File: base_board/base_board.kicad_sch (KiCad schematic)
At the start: 54 parts, among them J1 Conn_ARM_JTAG_SWD_20, J2 Conn_01x20_Pin, J3 Conn_01x20_Socket, SW1 SW_Push, U1 STM32F446ZEJx, U2 IS42S16400J-xT, U3 BMI270, U4 USB_C_Receptacle_USB2.0, U5 10p, U6 10p, U7 LD3985M33R_SOT23, Y1 Crystal_GND24

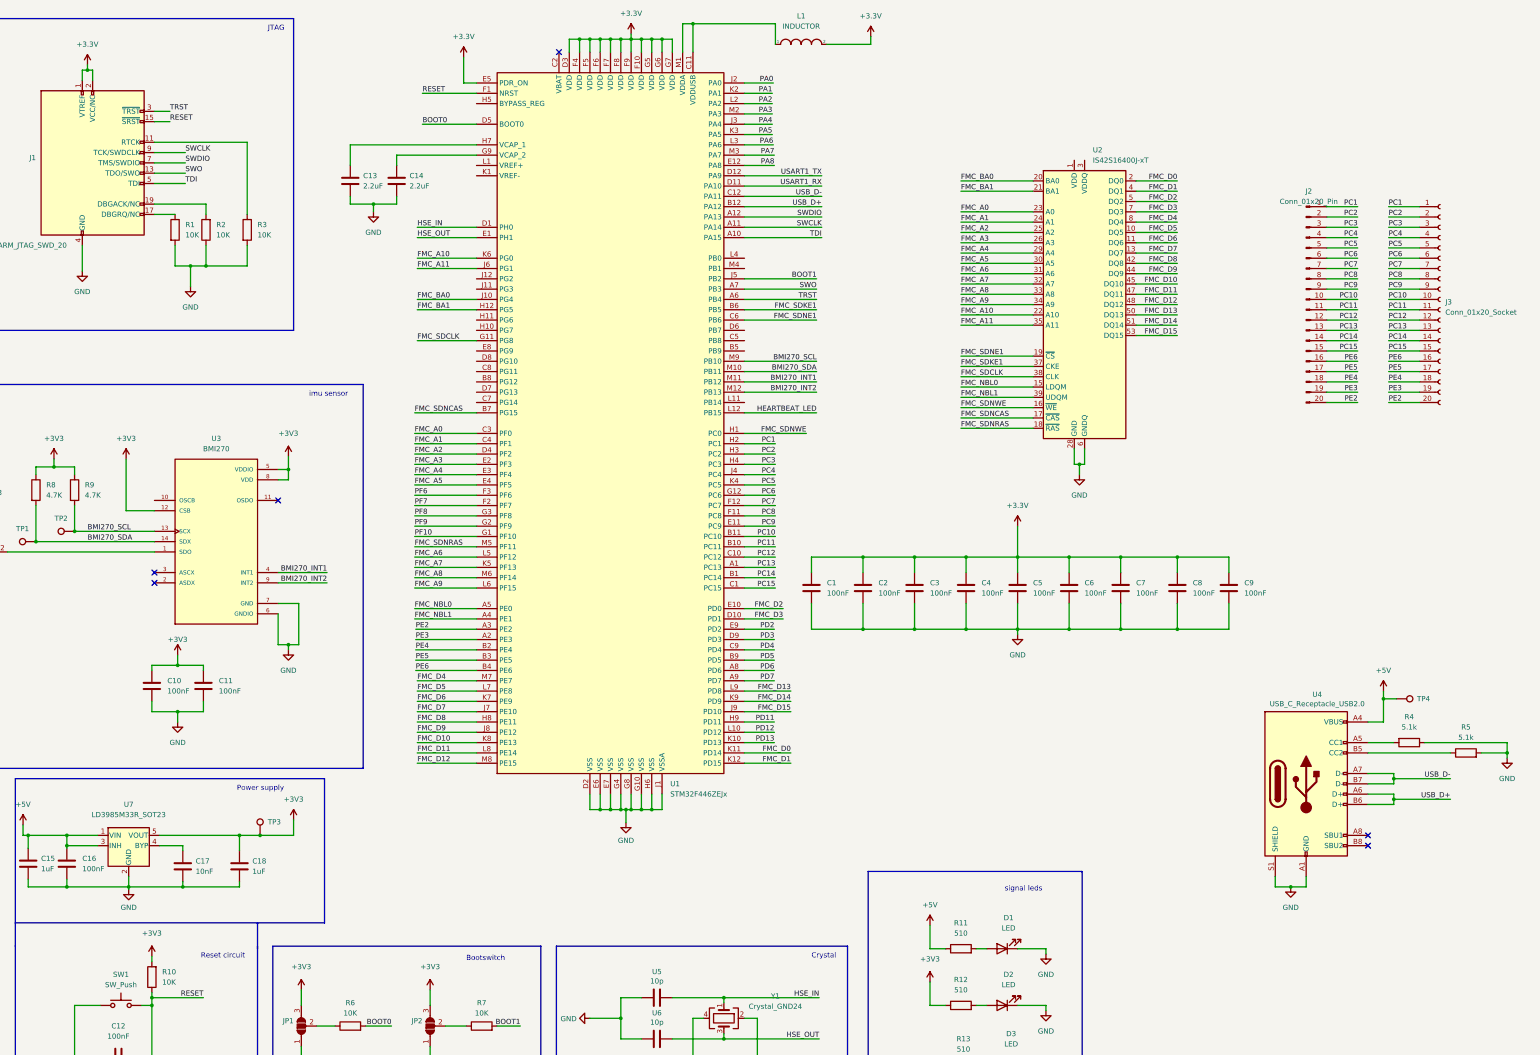
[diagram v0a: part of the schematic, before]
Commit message: Implemented SDRAM routing (#1)
* [pcb] completed sdram routing

* [pcb] added heartbeat led traces

* [pcb] completed routing except VDDUSB

* [pcb] changed routing for 5V power bus

* [pcb] fixed drc violation

* [pcb] added caps for VDDUSB

* [pcb] draft length matching

* [pcb] fixed length matching for sdram memory

* [view][pcb] toggled all layers for pcb

* [pcb] fixed power planes. Fixed traces shape

* [pcb] added review corrections

* [pcb] added M3 holes

* [pcb] added M3 holes

* [pcb] added onboard uart

* [pcb] added gnd+3v3 for uart socket

* [pcb][schematic] fixed VREF connection. Corrected the shape of the length matcher

* [project] updated fp-info-cache

* [pcb] fixed length matching pattern

* [pcb] placed sdram chip at 45 degree angle

* [project] updated fp-info cache
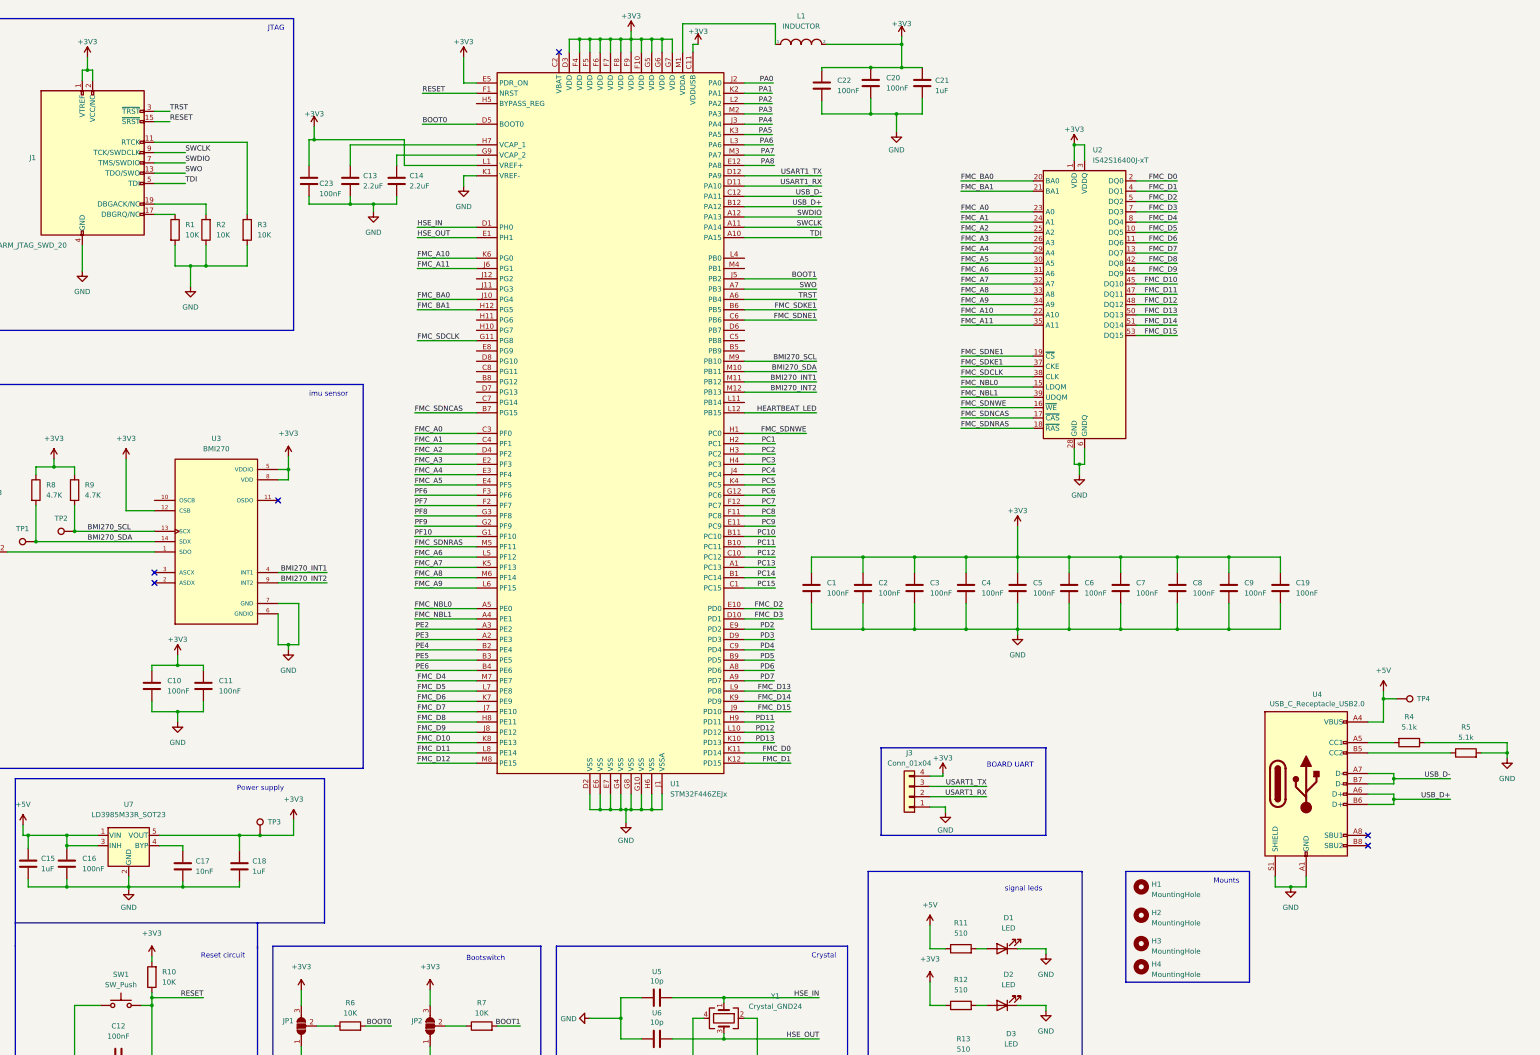
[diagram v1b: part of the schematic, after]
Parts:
- removed J2: Conn_01x20_Pin, Connector_PinHeader_2.54mm:PinHeader_1x20_P2.54mm_Vertical, symbol Connector:Conn_01x20_Pin
- removed J3: Conn_01x20_Socket, Connector_PinSocket_2.54mm:PinSocket_1x20_P2.54mm_Vertical, symbol Connector:Conn_01x20_Socket
- added C19, C20, C22, C23: 100nF, Capacitor_SMD:C_0603_1608Metric, symbol Device:C
- added C21: 1uF, Capacitor_SMD:C_0603_1608Metric, symbol Device:C
- added H1, H2, H3, H4: MountingHole, MountingHole:MountingHole_3.2mm_M3, symbol Mechanical:MountingHole
- added J3: Conn_01x04, Connector_PinHeader_2.54mm:PinHeader_1x04_P2.54mm_Vertical, symbol Connector_Generic:Conn_01x04
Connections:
- net +3.3V is gone; now on net +3V3: C1.1, C2.1, C3.1, C4.1, C5.1, C6.1, C7.1, C8.1, C9.1, J1.1 (VTREF), J1.2 (VCC/NC), L1.2, U1.D3 (VDD), U1.E5 (PDR_ON), U1.F10 (VDD), U1.F4 (VDD), U1.F5 (VDD), U1.F6 (VDD), U1.F7 (VDD), U1.F8 (VDD), U1.F9 (VDD), U1.G5 (VDD), U1.G6 (VDD), U1.G7 (VDD)
- net +3V3: now also U1.C11 (VDDUSB), U1.L1 (VREF+), U2.1 (VDD), U2.14 (VDD), U2.27 (VDD), U2.3 (VDDQ), U2.43 (VDDQ), U2.49 (VDDQ), U2.9 (VDDQ), C19.1, C20.1, C21.1, C22.1, C23.1, J3.4 (Pin_4)
- net GND: now also U1.K1 (VREF-), C19.2, C20.2, C21.2, C22.2, C23.2, J3.1 (Pin_1)
- net USART1_RX: now also J3.2 (Pin_2)
- net USART1_TX: now also J3.3 (Pin_3)
- net at L1.1, U1.M1 (VDDA): no longer U1.C11 (VDDUSB)
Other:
- note added: "BOARD UART"
- note added: "Mounts"
